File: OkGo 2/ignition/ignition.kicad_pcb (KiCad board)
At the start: 2 copper layers, 167.9 x 105.9 mm, 112 parts, among them K201 16A SPST, K202 16A SPST, K203 16A SPST, K204 16A SPST, K205 16A SPST, M3_MOUNT VAL**, P105 BATT, P107 ARM_LED, P109 BUZZ, P111 SMA, P201 CH3_LED, P203 CH3, P204 CH1_LED, P206 CH1, P207 CH4_LED, P209 CH4, P210 CH2_LED, P212 CH2, Q101 BSS138BK, Q201 BSS138BK, Q202 BSS138BK, Q203 BSS138BK, Q204 BSS138BK, Q205 BSS138BK, U103 SWD, U105 RFM95W, U106 STM32F071CBT6, U107 TSR 0.5-2433, Y101 8MHz

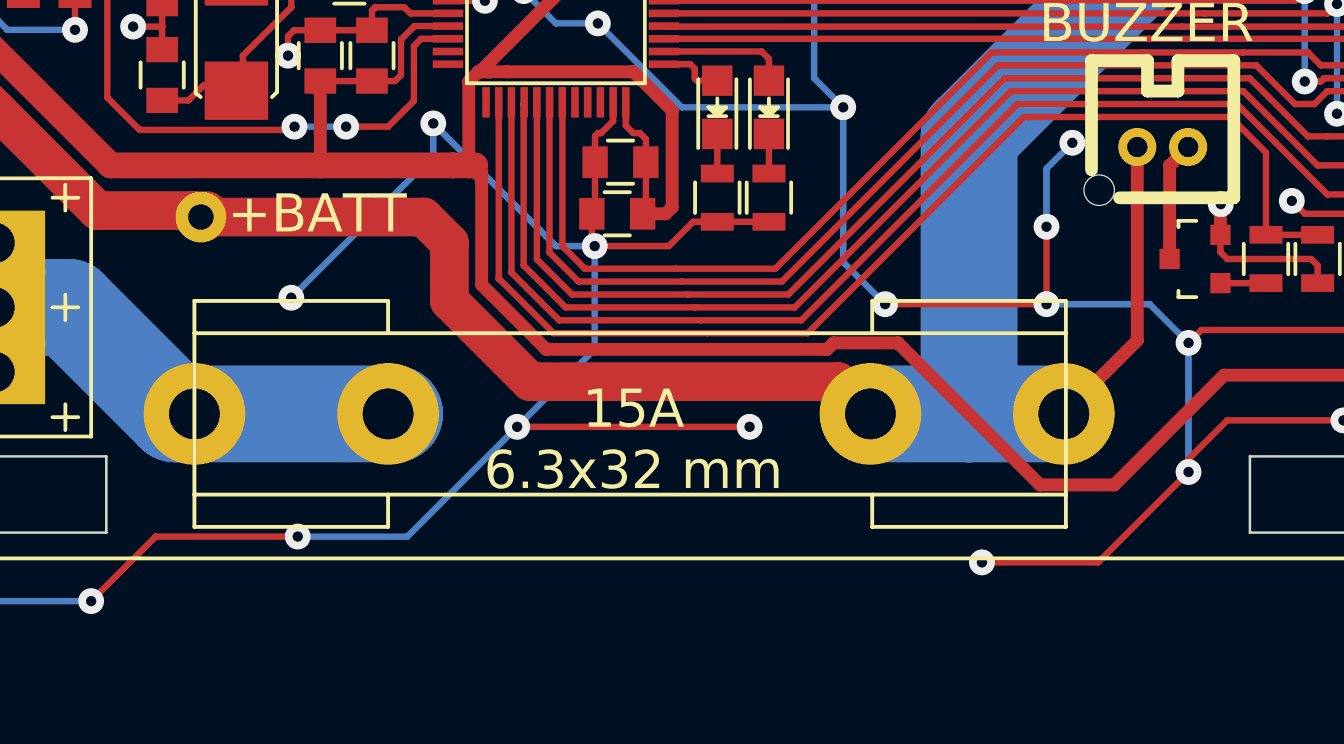
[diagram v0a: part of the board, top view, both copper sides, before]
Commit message: Moved vias from under fuse f/p
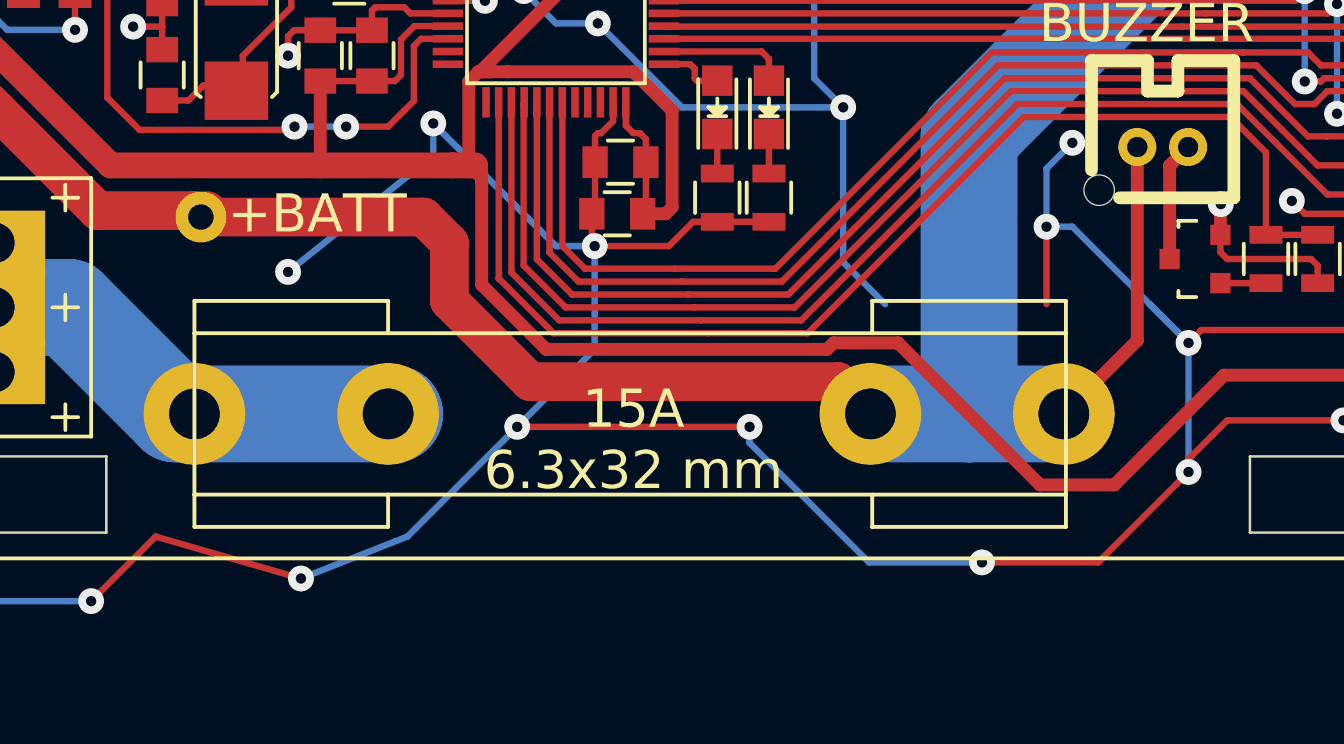
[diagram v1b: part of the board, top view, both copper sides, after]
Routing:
- net GND: track 1518.1 -> 1526.9 mm, vias 155 -> 153
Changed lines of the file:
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@@
     (thickness 1.6)
     (drawings 67)
-    (tracks 1585)
+    (tracks 1586)
     (zones 0)
     (modules 112)
@@
   (page A4)
   (layers
-    (0 F.Cu signal hide)
-    (31 B.Cu signal hide)
+    (0 F.Cu signal)
+    (31 B.Cu signal)
     (32 B.Adhes user)
     (33 F.Adhes user)
@@
   (segment (start 51.689 77.724) (end 52.451 78.486) (width 1.016) (layer F.Cu) (net 1))
   (segment (start 43.688 77.724) (end 43.688 77.851) (width 1.524) (layer F.Cu) (net 1))
+  (segment (start 94.996 92.964) (end 96.012 92.964) (width 0.254) (layer B.Cu) (net 2))
+  (segment (start 96.012 92.964) (end 100.584 97.536) (width 0.254) (layer B.Cu) (net 2))
+  (segment (start 83.312 100.838) (end 83.312 101.473) (width 0.254) (layer B.Cu) (net 2))
+  (via (at 74.168 100.838) (size 1.016) (drill 0.4064) (layers F.Cu B.Cu) (net 2))
+  (segment (start 74.168 100.838) (end 83.312 100.838) (width 0.254) (layer F.Cu) (net 2))
+  (via (at 83.312 100.838) (size 1.016) (drill 0.4064) (layers F.Cu B.Cu) (net 2))
+  (segment (start 97.028 106.172) (end 92.456 106.172) (width 0.254) (layer F.Cu) (net 2))
+  (via (at 92.456 106.172) (size 1.016) (drill 0.4064) (layers F.Cu B.Cu) (net 2))
+  (segment (start 97.028 106.172) (end 100.584 102.616) (width 0.254) (layer F.Cu) (net 2))
+  (segment (start 88.011 106.172) (end 92.456 106.172) (width 0.254) (layer B.Cu) (net 2))
+  (segment (start 83.312 101.473) (end 88.011 106.172) (width 0.254) (layer B.Cu) (net 2))
   (segment (start 154.305 102.87) (end 158.877 102.87) (width 0.254) (layer B.Cu) (net 2))
   (segment (start 157.988 99.187) (end 154.305 102.87) (width 0.254) (layer B.Cu) (net 2))
@@
   (via (at 57.404 107.696) (size 1.016) (drill 0.4064) (layers F.Cu B.Cu) (net 2))
   (segment (start 59.944 105.156) (end 57.404 107.696) (width 0.254) (layer F.Cu) (net 2))
-  (segment (start 65.532 105.156) (end 59.944 105.156) (width 0.254) (layer F.Cu) (net 2))
-  (via (at 65.532 105.156) (size 1.016) (drill 0.4064) (layers F.Cu B.Cu) (net 2))
-  (segment (start 69.85 105.156) (end 65.532 105.156) (width 0.254) (layer B.Cu) (net 2))
-  (segment (start 100.584 102.616) (end 97.028 106.172) (width 0.254) (layer F.Cu) (net 2))
-  (via (at 92.456 106.172) (size 1.016) (drill 0.4064) (layers F.Cu B.Cu) (net 2))
-  (segment (start 97.028 106.172) (end 92.456 106.172) (width 0.254) (layer F.Cu) (net 2))
+  (segment (start 65.659 106.807) (end 59.944 105.156) (width 0.254) (layer F.Cu) (net 2))
+  (via (at 65.659 106.807) (size 1.016) (drill 0.4064) (layers F.Cu B.Cu) (net 2))
+  (segment (start 69.85 105.156) (end 65.659 106.807) (width 0.254) (layer B.Cu) (net 2))
   (segment (start 100.584 102.616) (end 100.584 102.108) (width 0.254) (layer F.Cu) (net 2))
+  (segment (start 100.584 102.108) (end 102.108 100.584) (width 0.254) (layer F.Cu) (net 2))
+  (segment (start 102.108 100.584) (end 106.68 100.584) (width 0.254) (layer F.Cu) (net 2))
+  (via (at 106.68 100.584) (size 1.016) (drill 0.4064) (layers F.Cu B.Cu) (net 2))
+  (segment (start 106.68 100.584) (end 111.76 100.584) (width 0.254) (layer B.Cu) (net 2))
+  (segment (start 111.76 100.584) (end 112.268 101.092) (width 0.254) (layer B.Cu) (net 2))
+  (via (at 112.268 101.092) (size 1.016) (drill 0.4064) (layers F.Cu B.Cu) (net 2))
   (via (at 100.584 102.616) (size 1.016) (drill 0.4064) (layers F.Cu B.Cu) (net 2))
   (segment (start 100.584 97.536) (end 100.584 102.616) (width 0.254) (layer B.Cu) (net 2))
-  (via (at 112.268 101.092) (size 1.016) (drill 0.4064) (layers F.Cu B.Cu) (net 2))
-  (segment (start 111.76 100.584) (end 112.268 101.092) (width 0.254) (layer B.Cu) (net 2))
-  (segment (start 106.68 100.584) (end 111.76 100.584) (width 0.254) (layer B.Cu) (net 2))
-  (via (at 106.68 100.584) (size 1.016) (drill 0.4064) (layers F.Cu B.Cu) (net 2))
-  (segment (start 102.108 100.584) (end 106.68 100.584) (width 0.254) (layer F.Cu) (net 2))
-  (segment (start 100.584 102.108) (end 102.108 100.584) (width 0.254) (layer F.Cu) (net 2))
   (segment (start 108.204 93.472) (end 107.188 92.456) (width 0.254) (layer F.Cu) (net 2))
-  (segment (start 99.06 96.012) (end 100.584 97.536) (width 0.254) (layer B.Cu) (net 2))
-  (via (at 100.584 97.536) (size 1.016) (drill 0.4064) (layers F.Cu B.Cu) (net 2))
-  (segment (start 100.584 97.536) (end 101.092 97.028) (width 0.254) (layer F.Cu) (net 2))
-  (segment (start 101.092 97.028) (end 112.268 97.028) (width 0.254) (layer F.Cu) (net 2))
-  (via (at 112.268 97.028) (size 1.016) (drill 0.4064) (layers F.Cu B.Cu) (net 2))
-  (segment (start 112.268 97.028) (end 108.712 93.472) (width 0.254) (layer B.Cu) (net 2))
-  (segment (start 108.712 93.472) (end 108.204 93.472) (width 0.254) (layer B.Cu) (net 2))
-  (via (at 108.204 93.472) (size 1.016) (drill 0.4064) (layers F.Cu B.Cu) (net 2))
-  (via (at 94.996 96.012) (size 1.016) (drill 0.4064) (layers F.Cu B.Cu) (net 2))
-  (segment (start 94.996 96.012) (end 99.06 96.012) (width 0.254) (layer B.Cu) (net 2))
-  (via (at 104.648 91.948) (size 1.016) (drill 0.4064) (layers F.Cu B.Cu) (net 2))
-  (segment (start 105.156 92.456) (end 104.648 91.948) (width 0.254) (layer F.Cu) (net 2))
   (segment (start 107.188 92.456) (end 105.156 92.456) (width 0.254) (layer F.Cu) (net 2))
+  (segment (start 105.156 92.456) (end 104.648 91.948) (width 0.254) (layer F.Cu) (net 2))
+  (via (at 104.648 91.948) (size 1.016) (drill 0.4064) (layers F.Cu B.Cu) (net 2))
+  (via (at 108.204 93.472) (size 1.016) (drill 0.4064) (layers F.Cu B.Cu) (net 2))
+  (segment (start 108.712 93.472) (end 108.204 93.472) (width 0.254) (layer B.Cu) (net 2))
+  (segment (start 112.268 97.028) (end 108.712 93.472) (width 0.254) (layer B.Cu) (net 2))
+  (via (at 112.268 97.028) (size 1.016) (drill 0.4064) (layers F.Cu B.Cu) (net 2))
+  (segment (start 101.092 97.028) (end 112.268 97.028) (width 0.254) (layer F.Cu) (net 2))
+  (segment (start 100.584 97.536) (end 101.092 97.028) (width 0.254) (layer F.Cu) (net 2))
+  (via (at 100.584 97.536) (size 1.016) (drill 0.4064) (layers F.Cu B.Cu) (net 2))
+  (segment (start 99.06 96.012) (end 100.584 97.536) (width 0.254) (layer B.Cu) (net 2))
   (segment (start 107.696 77.724) (end 117.856 77.724) (width 0.254) (layer B.Cu) (net 2))
   (via (at 118.11 77.47) (size 1.016) (drill 0.4064) (layers F.Cu B.Cu) (net 2))
@@
   (segment (start 88.9 81.788) (end 94.488 81.788) (width 0.254) (layer B.Cu) (net 2))
   (segment (start 94.996 96.012) (end 94.996 92.964) (width 0.254) (layer F.Cu) (net 2))
-  (segment (start 94.996 96.012) (end 88.646 96.012) (width 0.254) (layer F.Cu) (net 2))
   (segment (start 86.995 94.361) (end 88.646 96.012) (width 0.254) (layer B.Cu) (net 2))
-  (via (at 88.646 96.012) (size 1.016) (drill 0.4064) (layers F.Cu B.Cu) (net 2))
   (via (at 86.995 88.265) (size 1.016) (drill 0.4064) (layers F.Cu B.Cu) (net 2))
   (segment (start 86.995 88.265) (end 86.995 94.361) (width 0.254) (layer B.Cu) (net 2))
@@
   (via (at 94.996 92.964) (size 1.016) (drill 0.4064) (layers F.Cu B.Cu) (net 2))
   (segment (start 77.216 93.726) (end 77.216 97.79) (width 0.254) (layer B.Cu) (net 2))
-  (via (at 83.312 100.838) (size 1.016) (drill 0.4064) (layers F.Cu B.Cu) (net 2))
-  (segment (start 74.168 100.838) (end 83.312 100.838) (width 0.254) (layer F.Cu) (net 2))
-  (via (at 74.168 100.838) (size 1.016) (drill 0.4064) (layers F.Cu B.Cu) (net 2))
   (segment (start 77.216 97.79) (end 74.168 100.838) (width 0.254) (layer B.Cu) (net 2))
   (segment (start 70.866 88.9) (end 70.866 90.17) (width 0.254) (layer B.Cu) (net 2))
@@
   (via (at 77.216 93.726) (size 1.016) (drill 0.4064) (layers F.Cu B.Cu) (net 2))
   (segment (start 77.216 93.726) (end 75.692 93.726) (width 0.254) (layer B.Cu) (net 2))
-  (via (at 65.278 95.758) (size 1.016) (drill 0.4064) (layers F.Cu B.Cu) (net 2))
-  (segment (start 70.866 90.17) (end 65.278 95.758) (width 0.254) (layer B.Cu) (net 2))
+  (via (at 65.151 94.742) (size 1.016) (drill 0.4064) (layers F.Cu B.Cu) (net 2))
+  (segment (start 70.866 90.17) (end 65.151 94.742) (width 0.254) (layer B.Cu) (net 2))
   (segment (start 46.355 84.836) (end 46.355 87.757) (width 0.254) (layer F.Cu) (net 2))
   (via (at 49.276 89.154) (size 1.016) (drill 0.4064) (layers F.Cu B.Cu) (net 2))
@@
   (segment (start 72.278 54.976) (end 69.596 57.658) (width 1.016) (layer F.Cu) (net 7))
   (segment (start 86.364 54.976) (end 84.964 54.976) (width 0.254) (layer F.Cu) (net 7))
+  (segment (start 91.948 89.408) (end 91.948 100.33) (width 3.81) (layer B.Cu) (net 8))
   (segment (start 150.147 94.488) (end 150.147 95.156) (width 0.254) (layer F.Cu) (net 8))
   (segment (start 150.942 95.951) (end 150.942 96.774) (width 0.254) (layer F.Cu) (net 8))
@@
   (segment (start 122.682 70.104) (end 111.252 70.104) (width 3.81) (layer B.Cu) (net 8))
   (segment (start 91.948 89.408) (end 111.252 70.104) (width 3.81) (layer B.Cu) (net 8))
-  (segment (start 91.948 89.408) (end 91.948 100.33) (width 3.81) (layer B.Cu) (net 8))
   (segment (start 61.722 92.583) (end 70.485 92.583) (width 1.524) (layer F.Cu) (net 8))
   (segment (start 70.485 92.583) (end 71.501 93.599) (width 1.524) (layer F.Cu) (net 8))
